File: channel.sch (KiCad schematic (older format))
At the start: 11 parts, among them J2 OUT, J3 CTRL, Q1 AO3400A, Q2 AO3400A, Q3 AO3400A, Q4 AO3400A, U2 MCP1416

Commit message: ready, but some cost-saving opportunities left
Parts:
- removed J2: OUT, TerminalBlock:TerminalBlock_bornier-3_P5.08mm, symbol Connector:Screw_Terminal_01x03
- removed J3: CTRL, Connector_PinHeader_2.54mm:PinHeader_1x02_P2.54mm_Vertical, symbol Connector_Generic:Conn_01x02
- removed NT1: ~, NetTie:NetTie-2_SMD_Pad0.5mm, symbol Device:NetTie_2
- removed Q4: AO3400A, Package_TO_SOT_SMD:SOT-23, symbol Transistor_FET:AO3400A
- added C13, C14, C15, C16, C5: 100n/50, Capacitor_SMD:C_0402_1005Metric_Pad0.74x0.62mm_HandSolder, symbol Device:C
- added R2: 4.7k, Resistor_SMD:R_0402_1005Metric, symbol Device:R
- added R3: 4.7k, Resistor_SMD:R_0402_1005Metric_Pad0.72x0.64mm_HandSolder, symbol Device:R
- R1: value 4.7k -> 120; footprint Resistor_SMD:R_0402_1005Metric -> Resistor_SMD:R_0402_1005Metric_Pad0.72x0.64mm_HandSolder; JLC C25900 -> C25079
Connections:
- net labels added: GATE_DRV, LOW_SIDE, PWM
- net labels removed: CTRL
- wire segments 18 -> 24
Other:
- note added: "C5/R2 can be replaced as needed for changing edge\n\nR2/C5 = 120Ω/100nF for fc=13.3kHz\n\nSee simulation PNGs for waveform\n\nRecommend driving with PWM frequency of 300-500Hz,\nideally with factors: (24/30/)72/120, i.e. 360Hz or 480Hz."
- note added: "\n\nAssuming 1A @ 12V (12Ω effective load), fc=32kHz\n\nAssuming 5A @ 24V (4.8Ω effective load), fc=80kHz"

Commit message: dual channel, cheaper (jellybean gate driver)
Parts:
- removed C4: 100n/50, Capacitor_SMD:C_0402_1005Metric, symbol Device:C
- removed U2: MCP1416, Package_TO_SOT_SMD:SOT-23-5, symbol Driver_FET:MCP1416
- added Q7, Q8: MMBT5551, Package_TO_SOT_SMD:SOT-23, symbol Transistor_BJT:MMBT5551L
- added Q9: MMBT5401, Package_TO_SOT_SMD:SOT-23, symbol Device:Q_PNP_BEC
- added R18, R20: 4.7k, Resistor_SMD:R_0402_1005Metric, symbol Device:R
- added R19: 1k, Resistor_SMD:R_0402_1005Metric, symbol Device:R
- C13, C14, C15, C16, C5: footprint Capacitor_SMD:C_0402_1005Metric_Pad0.74x0.62mm_HandSolder -> Capacitor_SMD:C_0402_1005Metric
- C3: value 1u/50 -> 100n/50; footprint Capacitor_SMD:C_0603_1608Metric -> Capacitor_SMD:C_0402_1005Metric_Pad0.74x0.62mm_HandSolder; JLC C15849 -> C307331
- R1: value 120 -> 4.7k; footprint Resistor_SMD:R_0402_1005Metric_Pad0.72x0.64mm_HandSolder -> Resistor_SMD:R_0402_1005Metric; JLC C25079 -> C25900
- R2: value 4.7k -> 120; footprint Resistor_SMD:R_0402_1005Metric -> Resistor_SMD:R_0402_1005Metric_Pad0.72x0.64mm_HandSolder; JLC C25900 -> C25079
- R3: footprint Resistor_SMD:R_0402_1005Metric_Pad0.72x0.64mm_HandSolder -> Resistor_SMD:R_0402_1005Metric
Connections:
- net labels removed: GATE_DRV
- wire segments 24 -> 30
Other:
- note added: "BJT: Vce(max) = 160V, hfe>100\nMOSFET: Vgc(max) = 12V"
- note added: "Base resistors reduce shoot-through that might occur\nif an output transistor saturates before a transition.\n\nEmitter resistors and shunt cap set output rise/fall time.\n\n120Ω/100nF for fc=13.3kHz\n\nRecommend driving with PWM frequency of 300-500Hz,\nideally with factors: (24/30/)72/120, i.e. 360Hz or 480Hz.\nThis should eliminate flicker in video."
- note added: "VDD≤12V"
- note removed: "C5/R2 can be replaced as needed for changing edge\n\nR2/C5 = 120Ω/100nF for fc=13.3kHz\n\nSee simulation PNGs for waveform\n\nRecommend driving with PWM frequency of 300-500Hz,\nideally with factors: (24/30/)72/120, i.e. 360Hz or 480Hz."
- note removed: "Max 18Vdd"
- moved on the sheet: C17, C18, C19, C20, Q4, Q5, Q6

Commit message: ready?
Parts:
- removed C13, C14, C15, C16: 100n/50, Capacitor_SMD:C_0402_1005Metric, symbol Device:C
- removed Q3: AO3400A, Package_TO_SOT_SMD:SOT-23, symbol Transistor_FET:AO3400A
- removed Q8: MMBT5551, Package_TO_SOT_SMD:SOT-23, symbol Transistor_BJT:MMBT5551L
- removed R1, R18, R3: 4.7k, Resistor_SMD:R_0402_1005Metric, symbol Device:R
- removed R19: 1k, Resistor_SMD:R_0402_1005Metric, symbol Device:R
- C3: value 100n/50 -> 3.3n; JLC C307331 -> C26404
- Q1, Q2: value AO3400A -> NTMS4807; footprint Package_TO_SOT_SMD:SOT-23 -> mark:NTMS-4807N-SOIC-8-3.9x4.9x1.27P; JLC C20917 -> C80851
- R2: value 120 -> 4.7k; JLC C25079 -> C25900
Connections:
- net PWM: now also Q7.1 (B), Q9.1 (B), R20.1
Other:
- note removed: "BJT: Vce(max) = 160V, hfe>100\nMOSFET: Vgc(max) = 12V"
- note removed: "Base resistors reduce shoot-through that might occur\nif an output transistor saturates before a transition.\n\nEmitter resistors and shunt cap set output rise/fall time.\n\n120Ω/100nF for fc=13.3kHz\n\nRecommend driving with PWM frequency of 300-500Hz,\nideally with factors: (24/30/)72/120, i.e. 360Hz or 480Hz.\nThis should eliminate flicker in video."
- note removed: "VDD≤12V"
- note removed: "\n\nAssuming 1A @ 12V (12Ω effective load), fc=32kHz\n\nAssuming 5A @ 24V (4.8Ω effective load), fc=80kHz"

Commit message: ready to order?
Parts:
- renumbered C5 to C10, C3 to C11, Q7 to Q1, Q9 to Q2, Q1 to Q3, Q2 to Q4, R2 to R8, R20 to R9
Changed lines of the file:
@@
 AR Path="/61C031A3/6203BADE" Ref="Q?"  Part="1"
 AR Path="/6203BADE" Ref="Q?"  Part="1"
-AR Path="/6202E846/6203BADE" Ref="Q1"  Part="1"
-AR Path="/620593AE/6203BADE" Ref="Q4"  Part="1"
-F 0 "Q4" H 1555 4246 50  0000 L CNN
+AR Path="/6202E846/6203BADE" Ref="Q3"  Part="1"
+AR Path="/620593AE/6203BADE" Ref="Q7"  Part="1"
+F 0 "Q7" H 1555 4246 50  0000 L CNN
 F 1 "NTMS4807" H 1555 4155 50  0000 L CNN
 F 2 "mark:NTMS-4807N-SOIC-8-3.9x4.9x1.27P" H 1550 4125 50  0001 L CIN
@@
 AR Path="/61C031A3/6203BAE5" Ref="Q?"  Part="1"
 AR Path="/6203BAE5" Ref="Q?"  Part="1"
-AR Path="/6202E846/6203BAE5" Ref="Q2"  Part="1"
-AR Path="/620593AE/6203BAE5" Ref="Q5"  Part="1"
-F 0 "Q5" H 2305 4246 50  0000 L CNN
+AR Path="/6202E846/6203BAE5" Ref="Q4"  Part="1"
+AR Path="/620593AE/6203BAE5" Ref="Q8"  Part="1"
+F 0 "Q8" H 2305 4246 50  0000 L CNN
 F 1 "NTMS4807" H 2305 4155 50  0000 L CNN
 F 2 "mark:NTMS-4807N-SOIC-8-3.9x4.9x1.27P" H 2300 4125 50  0001 L CIN
@@
 AR Path="/61C031A3/6203BB32" Ref="#PWR?"  Part="1"
 AR Path="/6203BB32" Ref="#PWR?"  Part="1"
-AR Path="/6202E846/6203BB32" Ref="#PWR011"  Part="1"
-AR Path="/620593AE/6203BB32" Ref="#PWR026"  Part="1"
-F 0 "#PWR026" H 1450 4250 50  0001 C CNN
+AR Path="/6202E846/6203BB32" Ref="#PWR029"  Part="1"
+AR Path="/620593AE/6203BB32" Ref="#PWR034"  Part="1"
+F 0 "#PWR034" H 1450 4250 50  0001 C CNN
 F 1 "GND" H 1455 4327 50  0000 C CNN
 F 2 "" H 1450 4500 50  0001 C CNN
@@
 Wire Wire Line
 	800  4200 1150 4200
-Text HLabel 6400 4000 2    50   UnSpc ~ 0
+Text HLabel 3350 4000 2    50   UnSpc ~ 0
 LOW_SIDE
 $Comp
@@
 AR Path="/61C031A1/61C0AE1D" Ref="#PWR?"  Part="1"
 AR Path="/61C031A3/61C0AE1D" Ref="#PWR?"  Part="1"
-AR Path="/6202E846/61C0AE1D" Ref="#PWR010"  Part="1"
-AR Path="/620593AE/61C0AE1D" Ref="#PWR022"  Part="1"
-F 0 "#PWR022" H 3000 2400 50  0001 C CNN
+AR Path="/6202E846/61C0AE1D" Ref="#PWR027"  Part="1"
+AR Path="/620593AE/61C0AE1D" Ref="#PWR032"  Part="1"
+F 0 "#PWR032" H 3000 2400 50  0001 C CNN
 F 1 "GND" H 3005 2477 50  0000 C CNN
 F 2 "" H 3000 2650 50  0001 C CNN
@@
 AR Path="/61C031A3/61C0ECF9" Ref="R?"  Part="1"
 AR Path="/61C0ECF9" Ref="R?"  Part="1"
-AR Path="/6202E846/61C0ECF9" Ref="R20"  Part="1"
-AR Path="/620593AE/61C0ECF9" Ref="R29"  Part="1"
-F 0 "R29" H 1530 2646 50  0000 R CNN
+AR Path="/6202E846/61C0ECF9" Ref="R9"  Part="1"
+AR Path="/620593AE/61C0ECF9" Ref="R11"  Part="1"
+F 0 "R11" H 1530 2646 50  0000 R CNN
 F 1 "4.7k" H 1530 2555 50  0000 R CNN
 F 2 "Resistor_SMD:R_0402_1005Metric" V 1530 2600 50  0001 C CNN
@@
 AR Path="/61C031A1/61C1051F" Ref="#PWR?"  Part="1"
 AR Path="/61C031A3/61C1051F" Ref="#PWR?"  Part="1"
-AR Path="/6202E846/61C1051F" Ref="#PWR012"  Part="1"
-AR Path="/620593AE/61C1051F" Ref="#PWR023"  Part="1"
-F 0 "#PWR023" H 1600 2500 50  0001 C CNN
+AR Path="/6202E846/61C1051F" Ref="#PWR028"  Part="1"
+AR Path="/620593AE/61C1051F" Ref="#PWR033"  Part="1"
+F 0 "#PWR033" H 1600 2500 50  0001 C CNN
 F 1 "GND" H 1605 2577 50  0000 C CNN
 F 2 "" H 1600 2750 50  0001 C CNN
@@
 AR Path="/61C031A1/61C20664" Ref="#PWR?"  Part="1"
 AR Path="/61C031A3/61C20664" Ref="#PWR?"  Part="1"
-AR Path="/6202E846/61C20664" Ref="#PWR02"  Part="1"
-AR Path="/620593AE/61C20664" Ref="#PWR013"  Part="1"
-F 0 "#PWR013" H 3900 2000 50  0001 C CNN
+AR Path="/6202E846/61C20664" Ref="#PWR026"  Part="1"
+AR Path="/620593AE/61C20664" Ref="#PWR031"  Part="1"
+F 0 "#PWR031" H 3900 2000 50  0001 C CNN
 F 1 "GND" H 3905 2077 50  0000 C CNN
 F 2 "" H 3900 2250 50  0001 C CNN
@@
 GATE
 $Comp
-L Transistor_BJT:MMBT5551L Q7
+L Transistor_BJT:MMBT5551L Q1
 U 1 1 61C0A1BB
 P 2900 1450
-AR Path="/6202E846/61C0A1BB" Ref="Q7"  Part="1"
-AR Path="/620593AE/61C0A1BB" Ref="Q10"  Part="1"
-F 0 "Q10" H 3091 1496 50  0000 L CNN
+AR Path="/6202E846/61C0A1BB" Ref="Q1"  Part="1"
+AR Path="/620593AE/61C0A1BB" Ref="Q5"  Part="1"
+F 0 "Q5" H 3091 1496 50  0000 L CNN
 F 1 "MMBT5551" H 3091 1405 50  0000 L CNN
 F 2 "Package_TO_SOT_SMD:SOT-23" H 3100 1375 50  0001 L CIN
@@
 AR Path="/61C031A3/61C5A1AF" Ref="R?"  Part="1"
 AR Path="/61C5A1AF" Ref="R?"  Part="1"
-AR Path="/6202E846/61C5A1AF" Ref="R2"  Part="1"
-AR Path="/620593AE/61C5A1AF" Ref="R24"  Part="1"
-F 0 "R24" V 3657 1950 50  0000 C CNN
+AR Path="/6202E846/61C5A1AF" Ref="R8"  Part="1"
+AR Path="/620593AE/61C5A1AF" Ref="R10"  Part="1"
+F 0 "R10" V 3657 1950 50  0000 C CNN
 F 1 "4.7k" V 3566 1950 50  0000 C CNN
 F 2 "Resistor_SMD:R_0402_1005Metric_Pad0.72x0.64mm_HandSolder" V 3380 1950 50  0001 C CNN
@@
 P 3900 2100
 AR Path="/61C61D09" Ref="C?"  Part="1"
-AR Path="/6202E846/61C61D09" Ref="C3"  Part="1"
-AR Path="/620593AE/61C61D09" Ref="C4"  Part="1"
-F 0 "C4" H 3785 2146 50  0000 R CNN
+AR Path="/6202E846/61C61D09" Ref="C11"  Part="1"
+AR Path="/620593AE/61C61D09" Ref="C13"  Part="1"
+F 0 "C13" H 3785 2146 50  0000 R CNN
 F 1 "3.3n" H 3785 2055 50  0000 R CNN
 F 2 "Capacitor_SMD:C_0402_1005Metric_Pad0.74x0.62mm_HandSolder" H 3938 1950 50  0001 C CNN
@@
 $EndComp
 $Comp
-L Device:Q_PNP_BEC Q9
+L Device:Q_PNP_BEC Q2
 U 1 1 61C4E023
 P 2900 2450
-AR Path="/6202E846/61C4E023" Ref="Q9"  Part="1"
-AR Path="/620593AE/61C4E023" Ref="Q12"  Part="1"
-F 0 "Q12" H 3091 2404 50  0000 L CNN
+AR Path="/6202E846/61C4E023" Ref="Q2"  Part="1"
+AR Path="/620593AE/61C4E023" Ref="Q6"  Part="1"
+F 0 "Q6" H 3091 2404 50  0000 L CNN
 F 1 "MMBT5401" H 3091 2495 50  0000 L CNN
 F 2 "Package_TO_SOT_SMD:SOT-23" H 3100 2550 50  0001 C CNN
@@
 AR Path="/61D142B7" Ref="C?"  Part="1"
 AR Path="/61B5C5B6/61D142B7" Ref="C?"  Part="1"
-AR Path="/6202E846/61D142B7" Ref="C5"  Part="1"
-AR Path="/620593AE/61D142B7" Ref="C10"  Part="1"
-F 0 "C10" H 1265 1346 50  0000 L CNN
+AR Path="/6202E846/61D142B7" Ref="C10"  Part="1"
+AR Path="/620593AE/61D142B7" Ref="C12"  Part="1"
+F 0 "C12" H 1265 1346 50  0000 L CNN
 F 1 "100n/50" H 1265 1255 50  0000 L CNN
 F 2 "Capacitor_SMD:C_0402_1005Metric" H 1188 1150 50  0001 C CNN
@@
 AR Path="/61C031A1/61D15BBF" Ref="#PWR?"  Part="1"
 AR Path="/61C031A3/61D15BBF" Ref="#PWR?"  Part="1"
-AR Path="/6202E846/61D15BBF" Ref="#PWR024"  Part="1"
-AR Path="/620593AE/61D15BBF" Ref="#PWR025"  Part="1"
-F 0 "#PWR025" H 1150 1200 50  0001 C CNN
+AR Path="/6202E846/61D15BBF" Ref="#PWR025"  Part="1"
+AR Path="/620593AE/61D15BBF" Ref="#PWR030"  Part="1"
+F 0 "#PWR030" H 1150 1200 50  0001 C CNN
 F 1 "GND" H 1155 1277 50  0000 C CNN
 F 2 "" H 1150 1450 50  0001 C CNN
@@
 	3900 1950 4950 1950
 Wire Wire Line
-	2200 4000 6400 4000
+	2200 4000 3350 4000
 $EndSCHEMATC

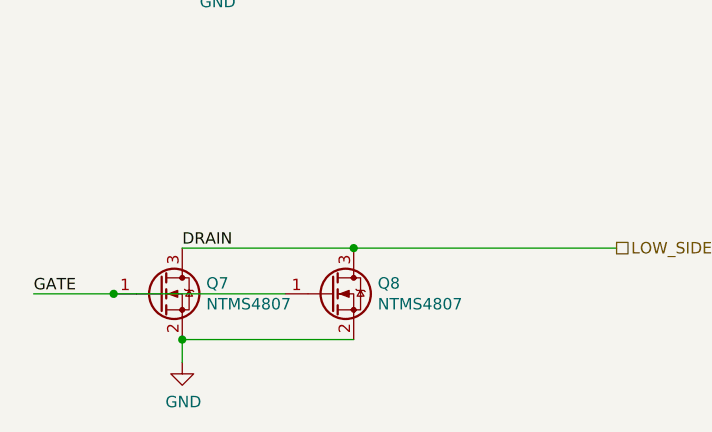
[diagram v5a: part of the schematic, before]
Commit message: moved screw terminals to edge of board, reduced stitching/thermal-via frequency
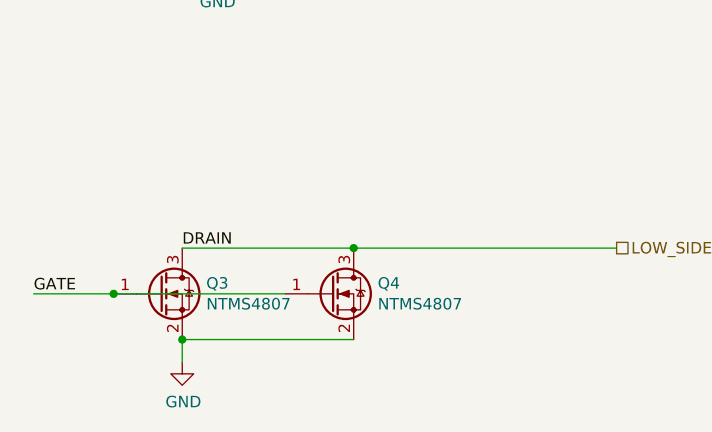
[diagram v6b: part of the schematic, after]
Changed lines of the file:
@@
 $Descr A4 11693 8268
 encoding utf-8
-Sheet 2 5
+Sheet 3 5
 Title ""
 Date ""
@@
 Comment4 ""
 $EndDescr
-$Comp
-L Transistor_FET:AO3400A Q?
-U 1 1 6203BADE
-P 1350 4200
-AR Path="/61B5C5B6/6203BADE" Ref="Q?"  Part="1"
-AR Path="/61C03040/6203BADE" Ref="Q?"  Part="1"
-AR Path="/61C031A1/6203BADE" Ref="Q?"  Part="1"
-AR Path="/61C031A3/6203BADE" Ref="Q?"  Part="1"
-AR Path="/6203BADE" Ref="Q?"  Part="1"
-AR Path="/6202E846/6203BADE" Ref="Q3"  Part="1"
-AR Path="/620593AE/6203BADE" Ref="Q7"  Part="1"
-F 0 "Q7" H 1555 4246 50  0000 L CNN
-F 1 "NTMS4807" H 1555 4155 50  0000 L CNN
-F 2 "mark:NTMS-4807N-SOIC-8-3.9x4.9x1.27P" H 1550 4125 50  0001 L CIN
-F 3 "https://datasheet.lcsc.com/lcsc/1809171608_ON-Semiconductor-NTMS4807NR2G_C80851.pdf" H 1350 4200 50  0001 L CNN
-F 4 "C80851" H 1350 4200 50  0001 C CNN "JLC"
-	1    1350 4200
-	1    0    0    -1
-$EndComp
-$Comp
-L Transistor_FET:AO3400A Q?
-U 1 1 6203BAE5
-P 2100 4200
-AR Path="/61B5C5B6/6203BAE5" Ref="Q?"  Part="1"
-AR Path="/61C03040/6203BAE5" Ref="Q?"  Part="1"
-AR Path="/61C031A1/6203BAE5" Ref="Q?"  Part="1"
-AR Path="/61C031A3/6203BAE5" Ref="Q?"  Part="1"
-AR Path="/6203BAE5" Ref="Q?"  Part="1"
-AR Path="/6202E846/6203BAE5" Ref="Q4"  Part="1"
-AR Path="/620593AE/6203BAE5" Ref="Q8"  Part="1"
-F 0 "Q8" H 2305 4246 50  0000 L CNN
-F 1 "NTMS4807" H 2305 4155 50  0000 L CNN
-F 2 "mark:NTMS-4807N-SOIC-8-3.9x4.9x1.27P" H 2300 4125 50  0001 L CIN
-F 3 "https://datasheet.lcsc.com/lcsc/1809171608_ON-Semiconductor-NTMS4807NR2G_C80851.pdf" H 2100 4200 50  0001 L CNN
-F 4 "C80851" H 2100 4200 50  0001 C CNN "JLC"
-	1    2100 4200
-	1    0    0    -1
-$EndComp
-Wire Wire Line
-	1450 4400 2200 4400
-Wire Wire Line
-	1450 4500 1450 4400
-Connection ~ 1450 4400
-Connection ~ 2200 4000
-Wire Wire Line
-	2200 4000 1450 4000
-Text Label 800  4200 0    50   ~ 0
-GATE
-Text Label 1450 4000 0    50   ~ 0
-DRAIN
-$Comp
-L power:GND #PWR?
-U 1 1 6203BB32
-P 1450 4500
-AR Path="/61B5C5B6/6203BB32" Ref="#PWR?"  Part="1"
-AR Path="/61C03040/6203BB32" Ref="#PWR?"  Part="1"
-AR Path="/61C031A1/6203BB32" Ref="#PWR?"  Part="1"
-AR Path="/61C031A3/6203BB32" Ref="#PWR?"  Part="1"
-AR Path="/6203BB32" Ref="#PWR?"  Part="1"
-AR Path="/6202E846/6203BB32" Ref="#PWR029"  Part="1"
-AR Path="/620593AE/6203BB32" Ref="#PWR034"  Part="1"
-F 0 "#PWR034" H 1450 4250 50  0001 C CNN
-F 1 "GND" H 1455 4327 50  0000 C CNN
-F 2 "" H 1450 4500 50  0001 C CNN
-F 3 "" H 1450 4500 50  0001 C CNN
-	1    1450 4500
-	1    0    0    -1
-$EndComp
-Wire Wire Line
-	1150 4200 1900 4200
-Wire Wire Line
-	800  4200 1150 4200
-Text HLabel 3350 4000 2    50   UnSpc ~ 0
-LOW_SIDE
 $Comp
 L power:GND #PWR?
@@
 	1    0    0    -1
 $EndComp
-Connection ~ 1150 4200
-Text Label 4950 1950 0    50   ~ 0
-GATE
 $Comp
 L Transistor_BJT:MMBT5551L Q1
@@
 Wire Wire Line
 	3900 1950 4950 1950
+Text Label 4950 1950 0    50   ~ 0
+GATE
+Text HLabel 3350 4000 2    50   UnSpc ~ 0
+LOW_SIDE
+$Comp
+L power:GND #PWR?
+U 1 1 6203BB32
+P 1450 4500
+AR Path="/61B5C5B6/6203BB32" Ref="#PWR?"  Part="1"
+AR Path="/61C03040/6203BB32" Ref="#PWR?"  Part="1"
+AR Path="/61C031A1/6203BB32" Ref="#PWR?"  Part="1"
+AR Path="/61C031A3/6203BB32" Ref="#PWR?"  Part="1"
+AR Path="/6203BB32" Ref="#PWR?"  Part="1"
+AR Path="/6202E846/6203BB32" Ref="#PWR029"  Part="1"
+AR Path="/620593AE/6203BB32" Ref="#PWR034"  Part="1"
+F 0 "#PWR029" H 1450 4250 50  0001 C CNN
+F 1 "GND" H 1455 4327 50  0000 C CNN
+F 2 "" H 1450 4500 50  0001 C CNN
+F 3 "" H 1450 4500 50  0001 C CNN
+	1    1450 4500
+	1    0    0    -1
+$EndComp
+Text Label 1450 4000 0    50   ~ 0
+DRAIN
+Text Label 800  4200 0    50   ~ 0
+GATE
+Wire Wire Line
+	1450 4500 1450 4400
+Wire Wire Line
+	1450 4400 2200 4400
 Wire Wire Line
 	2200 4000 3350 4000
+Wire Wire Line
+	2200 4000 1450 4000
+Connection ~ 2200 4000
+$Comp
+L Transistor_FET:AO3400A Q?
+U 1 1 6203BAE5
+P 2100 4200
+AR Path="/61B5C5B6/6203BAE5" Ref="Q?"  Part="1"
+AR Path="/61C03040/6203BAE5" Ref="Q?"  Part="1"
+AR Path="/61C031A1/6203BAE5" Ref="Q?"  Part="1"
+AR Path="/61C031A3/6203BAE5" Ref="Q?"  Part="1"
+AR Path="/6203BAE5" Ref="Q?"  Part="1"
+AR Path="/6202E846/6203BAE5" Ref="Q4"  Part="1"
+AR Path="/620593AE/6203BAE5" Ref="Q8"  Part="1"
+F 0 "Q4" H 2305 4246 50  0000 L CNN
+F 1 "NTMS4807" H 2305 4155 50  0000 L CNN
+F 2 "mark:NTMS-4807N-SOIC-8-3.9x4.9x1.27P" H 2300 4125 50  0001 L CIN
+F 3 "https://datasheet.lcsc.com/lcsc/1809171608_ON-Semiconductor-NTMS4807NR2G_C80851.pdf" H 2100 4200 50  0001 L CNN
+F 4 "C80851" H 2100 4200 50  0001 C CNN "JLC"
+	1    2100 4200
+	1    0    0    -1
+$EndComp
+Connection ~ 1450 4400
+Wire Wire Line
+	800  4200 1150 4200
+Wire Wire Line
+	1150 4200 1900 4200
+Connection ~ 1150 4200
+$Comp
+L Transistor_FET:AO3400A Q?
+U 1 1 6203BADE
+P 1350 4200
+AR Path="/61B5C5B6/6203BADE" Ref="Q?"  Part="1"
+AR Path="/61C03040/6203BADE" Ref="Q?"  Part="1"
+AR Path="/61C031A1/6203BADE" Ref="Q?"  Part="1"
+AR Path="/61C031A3/6203BADE" Ref="Q?"  Part="1"
+AR Path="/6203BADE" Ref="Q?"  Part="1"
+AR Path="/6202E846/6203BADE" Ref="Q3"  Part="1"
+AR Path="/620593AE/6203BADE" Ref="Q7"  Part="1"
+F 0 "Q3" H 1555 4246 50  0000 L CNN
+F 1 "NTMS4807" H 1555 4155 50  0000 L CNN
+F 2 "mark:NTMS-4807N-SOIC-8-3.9x4.9x1.27P" H 1550 4125 50  0001 L CIN
+F 3 "https://datasheet.lcsc.com/lcsc/1809171608_ON-Semiconductor-NTMS4807NR2G_C80851.pdf" H 1350 4200 50  0001 L CNN
+F 4 "C80851" H 1350 4200 50  0001 C CNN "JLC"
+	1    1350 4200
+	1    0    0    -1
+$EndComp
 $EndSCHEMATC
